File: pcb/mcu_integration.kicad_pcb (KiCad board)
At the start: 4 copper layers, 70 x 70 mm, 67 parts, among them IC1 TL7660IDGKR, IC2 TL081IDT, IC6 AD844_OPAMP_AL, IC7 FOD814_OPTO_AL, J1 Conn_01x05, J4 Conn_01x02, J5 DM3BT-DSF-PEJS, M1 MountingHole_Pad, M2 MountingHole_Pad, M3 MountingHole_Pad, M4 MountingHole_Pad, U1 STM32F103RBTx, U3 REF192_AL, U6 LM35DM

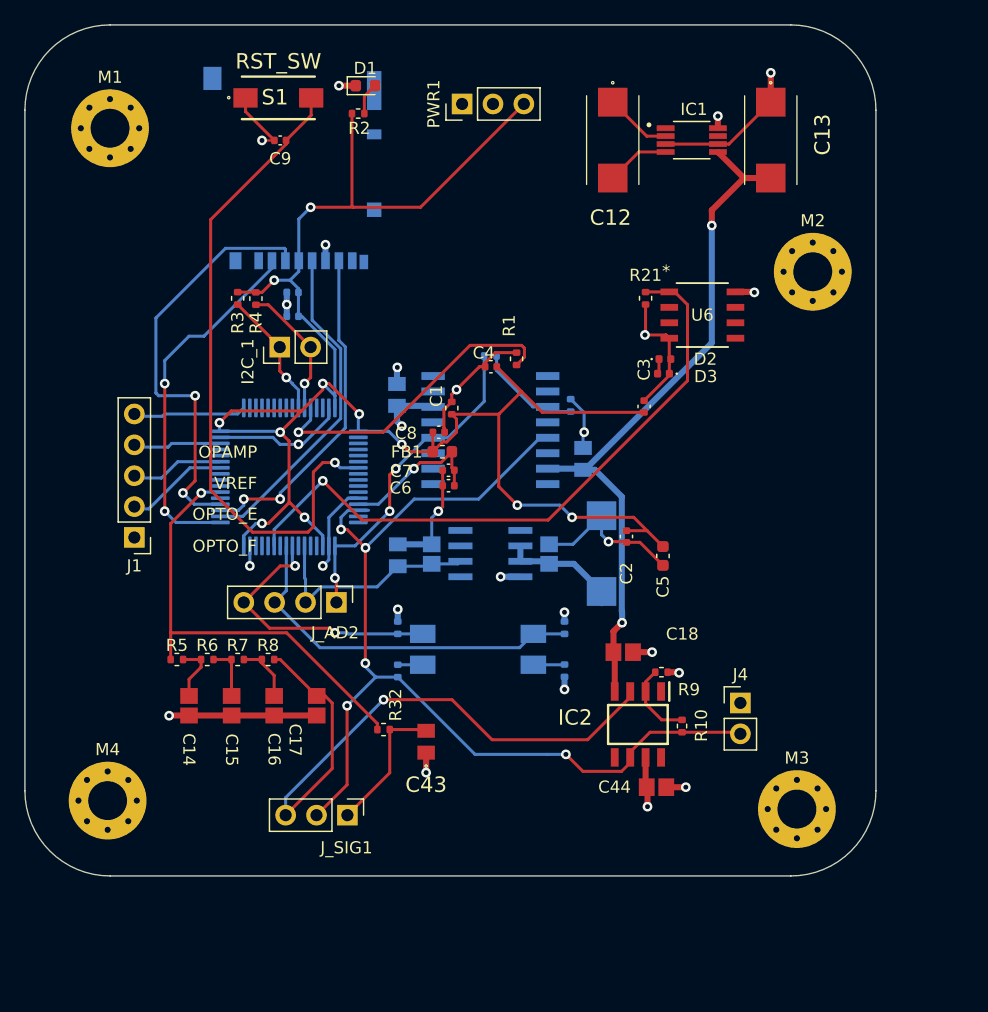
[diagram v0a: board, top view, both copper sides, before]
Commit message: Changed spacing between test ICs
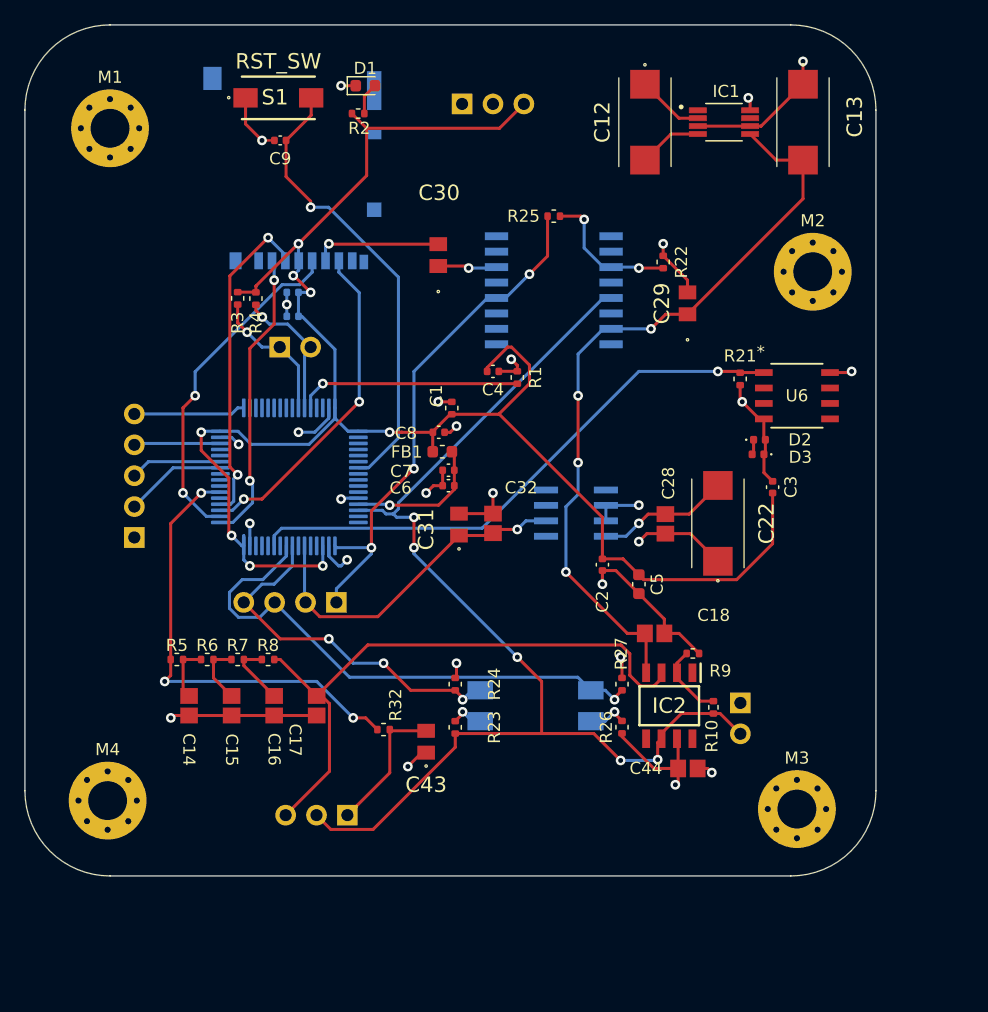
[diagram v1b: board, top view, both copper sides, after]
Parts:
- C22, C28, C29, C30, C31, C32, R22, R23, R24, R25, R26, R27: moved to F.Cu
- I2C_1, J1, J4, J_AD2, J_SIG1, PWR1: moved to B.Cu
- moved C29 15.4 mm to (158.0, 75.9)
- moved R22 14.0 mm to (156.0, 72.5)
- moved IC6 12.6 mm to (147.0, 74.8)
- moved R25 12.6 mm to (147.0, 68.7)
- moved C3 12.5 mm to (165.0, 91.0)
- moved C30 12.0 mm to (137.5, 71.9)
- moved R21 10.2 mm to (162.3, 82.1)
- moved D3 10.2 mm to (163.8, 88.3)
- moved D2 10.2 mm to (163.9, 87.1)
- moved U6 10.2 mm to (167.0, 83.5)
- moved C22 9.89 mm to (160.5, 94.0)
- moved C28 9.89 mm to (156.2, 94.0)
- moved U3 7.79 mm to (148.8, 93.2)
- moved IC7 6.63 mm to (145.5, 109.0)
- moved R26 6.63 mm to (152.6, 110.8)
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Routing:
- net /NRST: track 54.5 -> 37.8 mm
- net ADC1_IN3_OPAMP_AL: track 27.4 -> 42.9 mm
- net ADC1_IN15_OPTO_E_AL: track 30.9 -> 44.9 mm, vias 0 -> 1
- net ADC1_IN0_SINE: track 84.4 -> 96.1 mm
- net ADC1_IN6_VREF_AL: track 18.8 -> 28.2 mm, vias 0 -> 1
- net /SPI2_MOSI: track 35.4 -> 27.1 mm
- net /BOOT0: track 25.7 -> 18.4 mm
- net ADC1_IN14_OPTO_F_AL: track 23.0 -> 30.3 mm, vias 2 -> 3
- net +5V: track 22.5 -> 29.4 mm, vias 5 -> 6
- net ADC1_IN9_VREG_AL: track 53.2 -> 46.8 mm
- net /SPI2_CS_NSS: track 29.9 -> 24.2 mm
- net -5V Output: track 58.2 -> 62.4 mm, vias 2 -> 4
- net RC_OUTPUT: track 53.5 -> 50.0 mm, vias 1 -> 0
- net Net-(IC6--IN): track 8.69 -> 11.6 mm, vias 0 -> 2
- net GND: track 112.0 -> 109.9 mm, vias 22 -> 24
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
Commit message: changed 5 volt nets from 0.25mm to 0.5mm
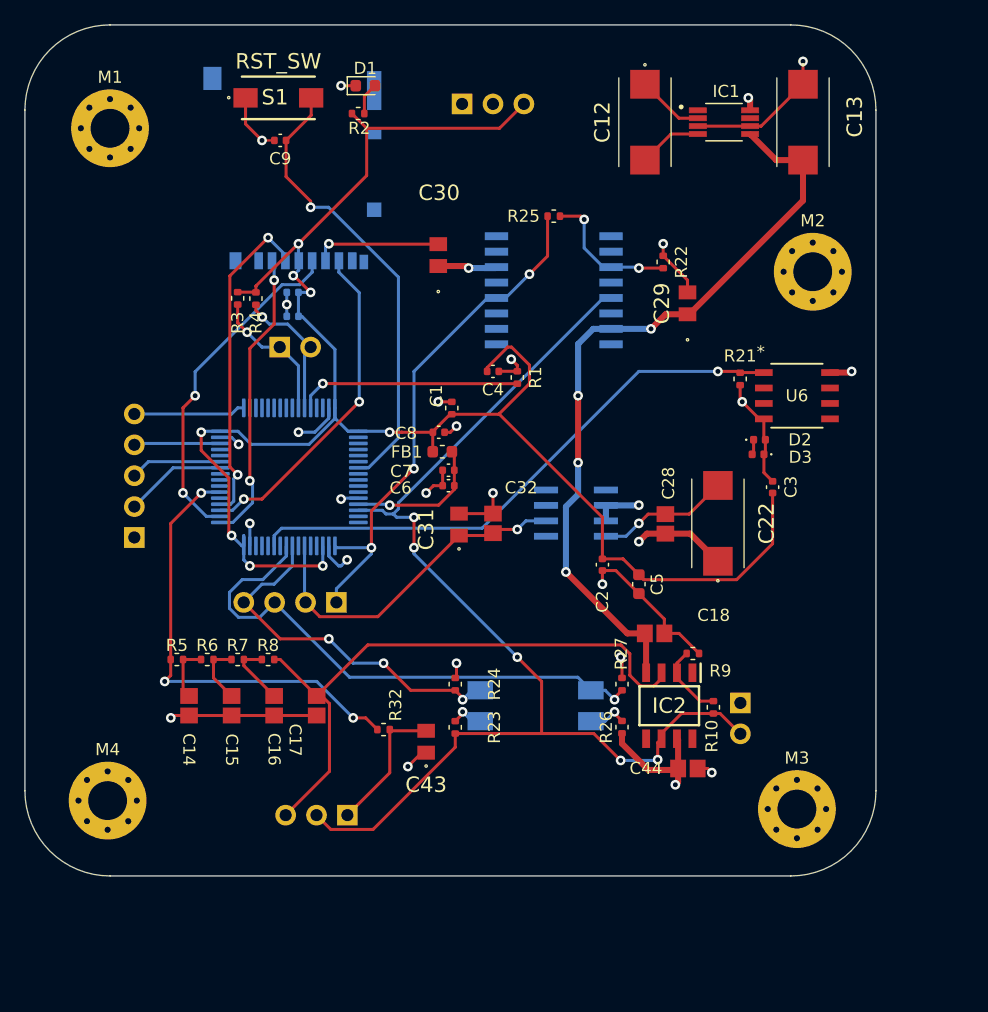
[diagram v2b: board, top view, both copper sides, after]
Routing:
- net -5V Output: track 62.4 -> 63.0 mm
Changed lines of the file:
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@@
 		(attr smd)
 		(fp_line
-			(start -0.153641 -0.38)
-			(end 0.153641 -0.38)
+			(start -0.153641 -0.5)
+			(end 0.153641 -0.5)
 			(stroke
 				(width 0.12)
@@
 		)
 		(fp_line
-			(start -0.153641 0.38)
-			(end 0.153641 0.38)
+			(start -0.153641 0.5)
+			(end 0.153641 0.5)
 			(stroke
 				(width 0.12)
@@
 		(attr smd)
 		(fp_line
-			(start -0.153641 -0.38)
-			(end 0.153641 -0.38)
+			(start -0.153641 -0.5)
+			(end 0.153641 -0.5)
 			(stroke
 				(width 0.12)
@@
 		)
 		(fp_line
-			(start -0.153641 0.38)
-			(end 0.153641 0.38)
+			(start -0.153641 0.5)
+			(end 0.153641 0.5)
 			(stroke
 				(width 0.12)
@@
 		(attr smd)
 		(fp_line
-			(start -0.153641 -0.38)
-			(end 0.153641 -0.38)
+			(start -0.153641 -0.5)
+			(end 0.153641 -0.5)
 			(stroke
 				(width 0.12)
@@
 		)
 		(fp_line
-			(start -0.153641 0.38)
-			(end 0.153641 0.38)
+			(start -0.153641 0.5)
+			(end 0.153641 0.5)
 			(stroke
 				(width 0.12)
@@
 		(attr smd)
 		(fp_line
-			(start -0.107836 -0.36)
-			(end 0.107836 -0.36)
+			(start -0.107836 -0.5)
+			(end 0.107836 -0.5)
 			(stroke
 				(width 0.12)
@@
 		)
 		(fp_line
-			(start -0.107836 0.36)
-			(end 0.107836 0.36)
+			(start -0.107836 0.5)
+			(end 0.107836 0.5)
 			(stroke
 				(width 0.12)
@@
 	)
 	(segment
+		(start 158.15 76.8)
+		(end 158 76.8)
+		(width 0.5)
+		(layer "F.Cu")
+		(net 20)
+	)
+	(segment
 		(start 154.49 103.05)
 		(end 153.05 103.05)
-		(width 0.25)
+		(width 0.5)
 		(layer "F.Cu")
 		(net 20)
 	)
 	(segment
-		(start 154.595 103.155)
-		(end 154.49 103.05)
-		(width 0.25)
+		(start 167.5 67.45)
+		(end 158.15 76.8)
+		(width 0.5)
 		(layer "F.Cu")
 		(net 20)
 	)
 	(segment
-		(start 167.5 64.12)
-		(end 167.5 67.3)
-		(width 0.25)
+		(start 154.595 103.155)
+		(end 154.49 103.05)
+		(width 0.5)
 		(layer "F.Cu")
 		(net 20)
@@
 		(start 153.05 103.05)
 		(end 148 98)
-		(width 0.25)
+		(width 0.5)
 		(layer "F.Cu")
 		(net 20)
@@
 		(start 158 76.8)
 		(end 156.2 76.8)
-		(width 0.25)
+		(width 0.5)
 		(layer "F.Cu")
 		(net 20)
@@
 		(start 156.2 76.8)
 		(end 155 78)
-		(width 0.25)
+		(width 0.5)
 		(layer "F.Cu")
 		(net 20)
 	)
 	(segment
-		(start 165.295 64.12)
-		(end 163.15 61.975)
-		(width 0.25)
+		(start 163.19 62.015)
+		(end 163.15 62.015)
+		(width 0.5)
 		(layer "F.Cu")
 		(net 20)
@@
 		(start 149 89)
 		(end 149 83.5)
-		(width 0.25)
+		(width 0.5)
+		(layer "F.Cu")
+		(net 20)
+	)
+	(segment
+		(start 167.5 64.12)
+		(end 167.5 67.45)
+		(width 0.5)
 		(layer "F.Cu")
 		(net 20)
@@
 		(start 154.595 106.288)
 		(end 154.595 103.155)
-		(width 0.25)
+		(width 0.5)
 		(layer "F.Cu")
 		(net 20)
 	)
 	(segment
-		(start 167.5 64.12)
-		(end 165.295 64.12)
-		(width 0.25)
+		(start 165.295 64.12)
+		(end 163.19 62.015)
+		(width 0.5)
 		(layer "F.Cu")
 		(net 20)
 	)
 	(segment
-		(start 167.5 67.3)
-		(end 158 76.8)
-		(width 0.25)
+		(start 167.5 64.12)
+		(end 165.295 64.12)
+		(width 0.5)
 		(layer "F.Cu")
 		(net 20)
@@
 	)
 	(segment
-		(start 149 80.0745)
-		(end 151.0745 78)
-		(width 0.25)
+		(start 150.2495 78)
+		(end 151.712 78)
+		(width 0.5)
 		(layer "B.Cu")
 		(net 20)
@@
 		(start 148 98)
 		(end 148 92.621202)
-		(width 0.25)
+		(width 0.5)
 		(layer "B.Cu")
 		(net 20)
@@
 		(start 149 91.621202)
 		(end 149 89)
-		(width 0.25)
+		(width 0.5)
 		(layer "B.Cu")
 		(net 20)
@@
 		(start 155 78)
 		(end 151.712 78)
-		(width 0.25)
+		(width 0.5)
 		(layer "B.Cu")
 		(net 20)
 	)
 	(segment
-		(start 151.0745 78)
-		(end 151.712 78)
-		(width 0.25)
+		(start 149 83.5)
+		(end 149 79.2495)
+		(width 0.5)
 		(layer "B.Cu")
 		(net 20)
@@
 		(start 148 92.621202)
 		(end 149 91.621202)
-		(width 0.25)
+		(width 0.5)
 		(layer "B.Cu")
 		(net 20)
 	)
 	(segment
-		(start 149 83.5)
-		(end 149 80.0745)
-		(width 0.25)
+		(start 149 79.2495)
+		(end 150.2495 78)
+		(width 0.5)
 		(layer "B.Cu")
 		(net 20)
@@
 	)
 	(segment
+		(start 157.227201 114.16)
+		(end 157.102201 114.285)
+		(width 0.5)
+		(layer "F.Cu")
+		(net 41)
+	)
+	(segment
 		(start 139.833 72.833)
 		(end 140 73)
-		(width 0.25)
+		(width 0.5)
 		(layer "F.Cu")
 		(net 41)
@@
 		(start 157.227201 114.16)
 		(end 157.227201 111.804201)
-		(width 0.25)
+		(width 0.5)
 		(layer "F.Cu")
 		(net 41)
 	)
 	(segment
-		(start 163.15 60.025)
-		(end 163.15 59.15)
-		(width 0.25)
+		(start 163.15 59.15)
+		(end 163.15 59.985)
+		(width 0.5)
+		(layer "F.Cu")
+		(net 41)
+	)
+	(segment
+		(start 154.785 114.285)
+		(end 152.612 112.112)
+		(width 0.5)
 		(layer "F.Cu")
 		(net 41)
@@
 		(start 156.182 94.843598)
 		(end 158.223598 94.843598)
-		(width 0.25)
+		(width 0.5)
 		(layer "F.Cu")
 		(net 41)
@@
 		(start 158.223598 94.843598)
 		(end 160.5 97.12)
-		(width 0.25)
+		(width 0.5)
 		(layer "F.Cu")
 		(net 41)
@@
 		(start 157.227201 114.16)
 		(end 157.227201 115.272799)
-		(width 0.25)
+		(width 0.5)
 		(layer "F.Cu")
 		(net 41)
@@
 		(start 157.227201 111.804201)
 		(end 157.135 111.712)
-		(width 0.25)
+		(width 0.5)
 		(layer "F.Cu")
 		(net 41)
@@
 		(start 137.5 72.833)
 		(end 139.833 72.833)
-		(width 0.25)
-		(layer "F.Cu")
-		(net 41)
-	)
-	(segment
-		(start 152.612 111.27)
-		(end 152.612 111.539999)
-		(width 0.25)
+		(width 0.5)
 		(layer "F.Cu")
 		(net 41)
@@
 		(start 157.227201 115.272799)
 		(end 157 115.5)
-		(width 0.25)
+		(width 0.5)
 		(layer "F.Cu")
 		(net 41)
@@
 		(start 171.405 81.595)
 		(end 171.5 81.5)
-		(width 0.25)
+		(width 0.5)
 		(layer "F.Cu")
 		(net 41)
@@
 		(start 169.721348 81.595)
 		(end 171.405 81.595)
-		(width 0.25)
+		(width 0.5)
 		(layer "F.Cu")
 		(net 41)
 	)
 	(segment
-		(start 152.612 111.539999)
-		(end 155.232001 114.16)
-		(width 0.25)
+		(start 163.15 59.15)
+		(end 163 59)
+		(width 0.5)
 		(layer "F.Cu")
 		(net 41)
 	)
 	(segment
-		(start 163.15 59.15)
-		(end 163 59)
-		(width 0.25)
+		(start 157.102201 114.285)
+		(end 154.785 114.285)
+		(width 0.5)
 		(layer "F.Cu")
 		(net 41)
 	)
 	(segment
-		(start 156.182 94.843598)
-		(end 154.656402 94.843598)
-		(width 0.25)
+		(start 152.612 112.112)
+		(end 152.612 111.27)
+		(width 0.5)
 		(layer "F.Cu")
 		(net 41)
 	)
 	(segment
-		(start 155.232001 114.16)
-		(end 157.227201 114.16)
-		(width 0.25)
+		(start 156.182 94.843598)
+		(end 154.656402 94.843598)
+		(width 0.5)
 		(layer "F.Cu")
 		(net 41)
@@
 		(start 154.656402 94.843598)
 		(end 154 95.5)
-		(width 0.25)
+		(width 0.5)
 		(layer "F.Cu")
 		(net 41)
@@
 		(start 151.2898 92.521402)
 		(end 151.2898 93.791402)
-		(width 0.25)
+		(width 0.5)
 		(layer "B.Cu")
 		(net 41)
@@
 		(start 142.208 73)
 		(end 142.288 72.92)
-		(width 0.25)
+		(width 0.5)
 		(layer "B.Cu")
 		(net 41)
@@
 		(start 140 73)
 		(end 142.208 73)
-		(width 0.25)
+		(width 0.5)
 		(layer "B.Cu")
 		(net 41)
@@
 		(start 151.2898 92.521402)
 		(end 153.978598 92.521402)
-		(width 0.25)
+		(width 0.5)
 		(layer "B.Cu")
 		(net 41)
@@
 		(start 153.978598 92.521402)
 		(end 154 92.5)
-		(width 0.25)
+		(width 0.5)
 		(layer "B.Cu")
 		(net 41)

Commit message: Fixed pin labels
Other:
- board text added: "SWCLK"
- board text added: "SWDIO"
- board text added: "USART1_RX"
- board text added: "USART1_TX"
- board text removed: "OPAMP"
- board text removed: "OPTO_E"
- board text removed: "OPTO_F"
- board text removed: "VREF"
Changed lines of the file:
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@@
 		(layer "Edge.Cuts")
 	)
-	(gr_text "OPTO_F"
-		(at 110.28 93.17 -0)
+	(gr_text "USART1_TX"
+		(at 110.5 93.17 0)
 		(layer "B.SilkS")
 		(effects
 			(font
-				(size 1 1)
+				(size 1 0.75)
 				(thickness 0.15)
 			)
@@
 		)
 	)
-	(gr_text "OPAMP"
-		(at 109.8 85.43 -0)
+	(gr_text "SWCLK"
+		(at 109.8 85.43 0)
 		(layer "B.SilkS")
 		(effects
 			(font
-				(size 1 1)
+				(size 1 0.75)
 				(thickness 0.15)
 			)
@@
 		)
 	)
-	(gr_text "OPTO_E"
-		(at 110.29 90.54 -0)
+	(gr_text "USART1_RX"
+		(at 110.5 90.54 0)
 		(layer "B.SilkS")
 		(effects
 			(font
-				(size 1 1)
+				(size 1 0.75)
 				(thickness 0.15)
 			)
@@
 		)
 	)
-	(gr_text "VREF"
-		(at 108.5 88 -0)
+	(gr_text "SWDIO"
+		(at 109.5 88 0)
 		(layer "B.SilkS")
 		(effects
 			(font
-				(size 1 1)
+				(size 1 0.75)
 				(thickness 0.15)
 			)

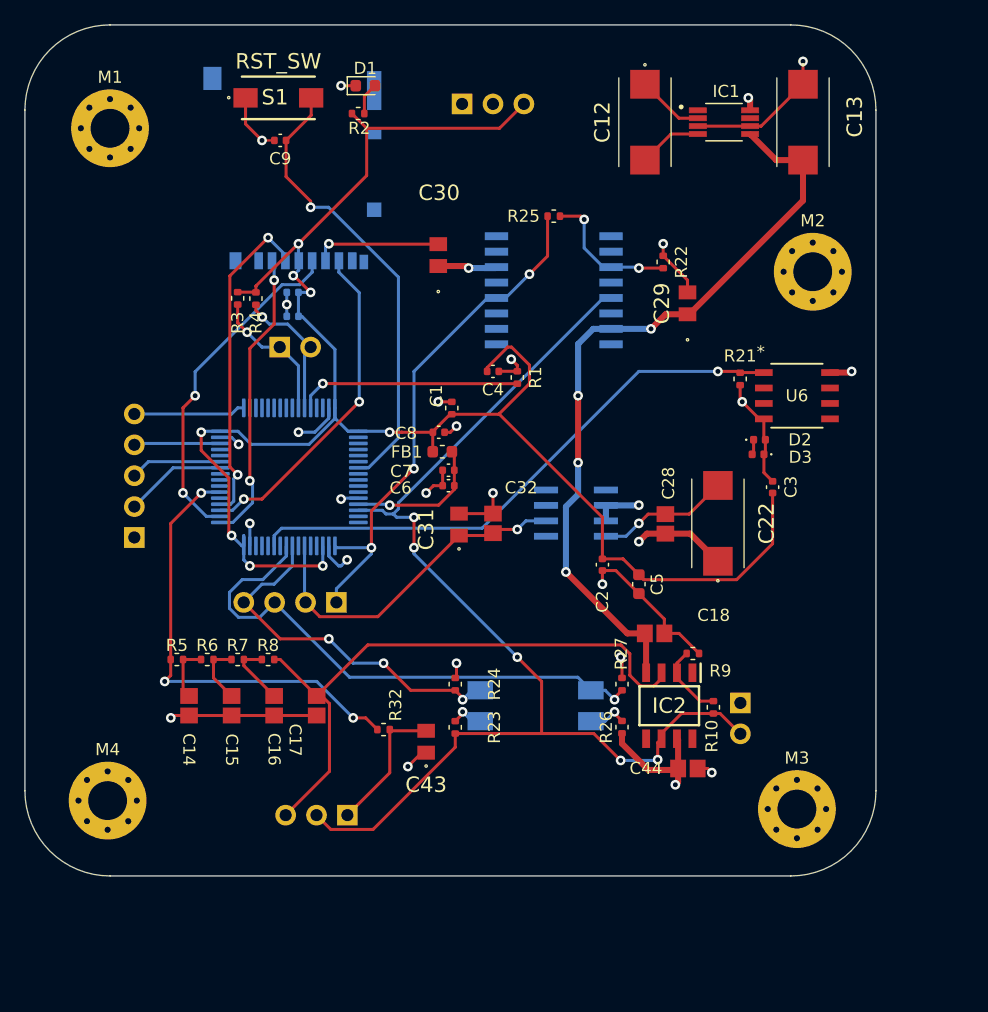
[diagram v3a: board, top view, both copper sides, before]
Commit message: Ran DFM and made adjustments accordingly
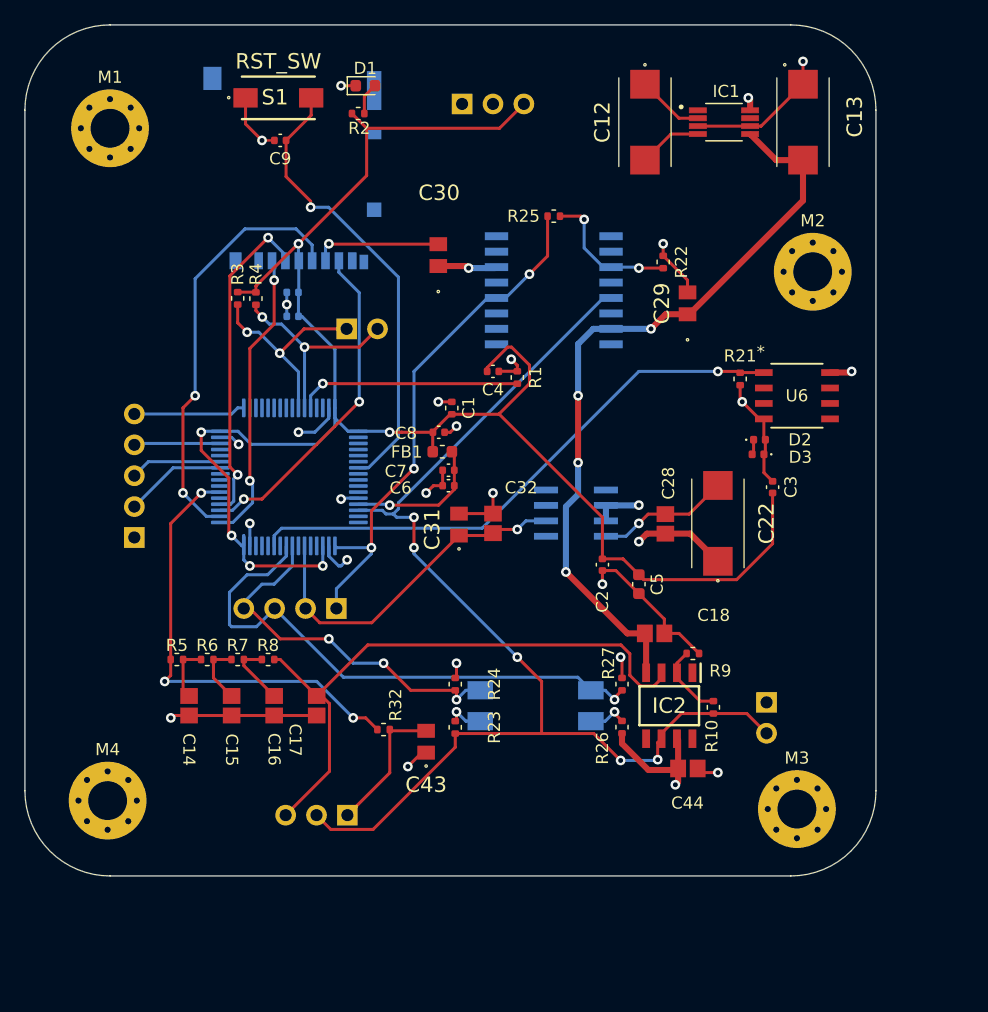
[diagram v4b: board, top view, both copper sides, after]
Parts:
- moved I2C_1 5.70 mm to (130.0, 78.0)
- moved J4 2.15 mm to (164.5, 108.7)
- moved J_AD2 0.50 mm to (129.1, 101.0)
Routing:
- net /SPI2_SCK: track 28.2 -> 35.1 mm
- net OBC_I2C_SCL: track 11.4 -> 17.5 mm, vias 1 -> 2
- net OBC_I2C_SDA: track 11.4 -> 17.3 mm, vias 1 -> 2
- net ADC1_IN0_SINE: track 96.1 -> 98.2 mm
- net 3.3V Output: track 148.3 -> 146.8 mm, vias 8 -> 6
- net ADC1_IN15_OPTO_E_AL: track 44.9 -> 45.9 mm
- net ADC1_IN6_VREF_AL: track 28.2 -> 29.0 mm
- net GND: track 109.9 -> 110.4 mm
- net ADC1_IN3_OPAMP_AL: track 42.9 -> 43.4 mm
